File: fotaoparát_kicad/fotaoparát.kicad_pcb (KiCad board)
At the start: 4 copper layers, 115.5 x 68 mm, 64 parts, among them J1 Conn_01x01_Pin, J10 Conn_01x01_Pin, J11 Conn_01x01_Pin, J12 Conn_01x01_Pin, J13 Micro_SD_Card_Det2, J2 Conn_01x01_Pin, J3 Conn_01x01_Pin, J4 Conn_01x01_Pin, J5 Conn_01x01_Pin, J6 Conn_01x01_Pin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

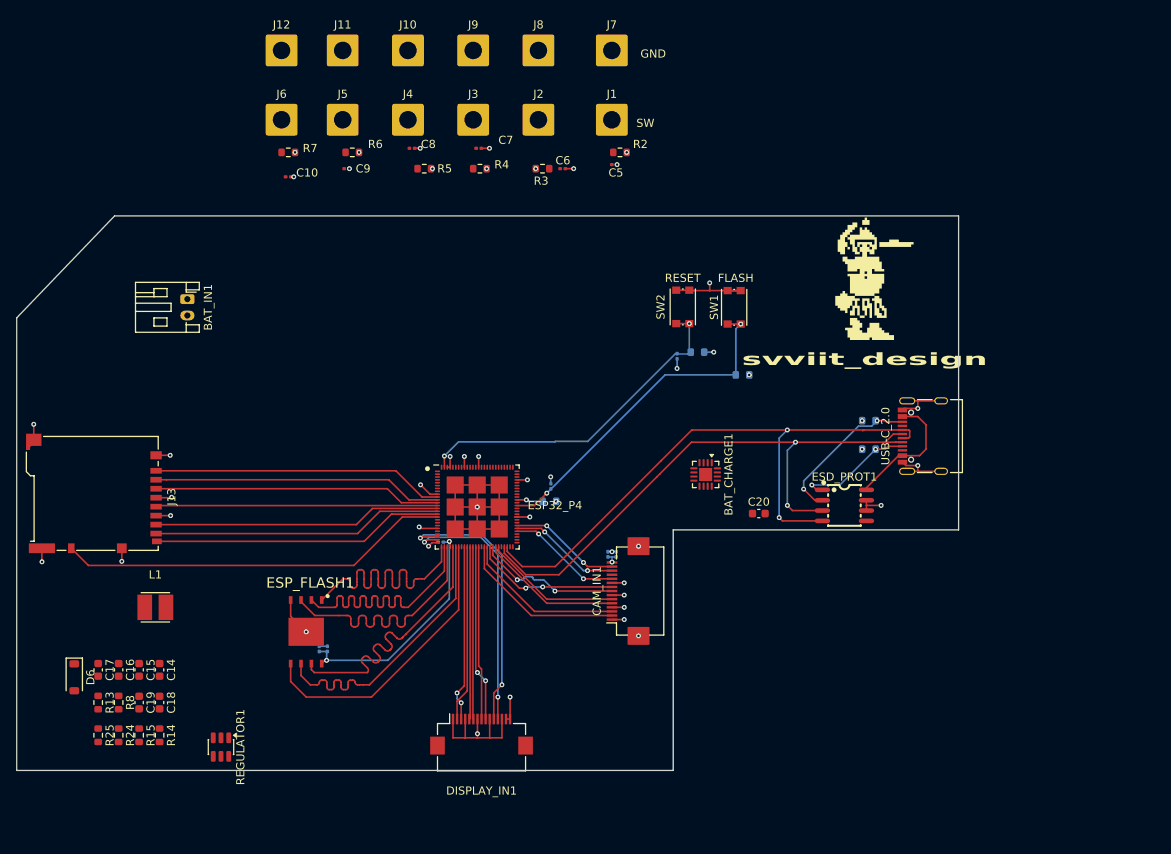
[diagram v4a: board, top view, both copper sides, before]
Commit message: Predelani 80 % routingu pro optimalizaci mista na desce, a predelani napajeni do 7,2V akumulatoru.
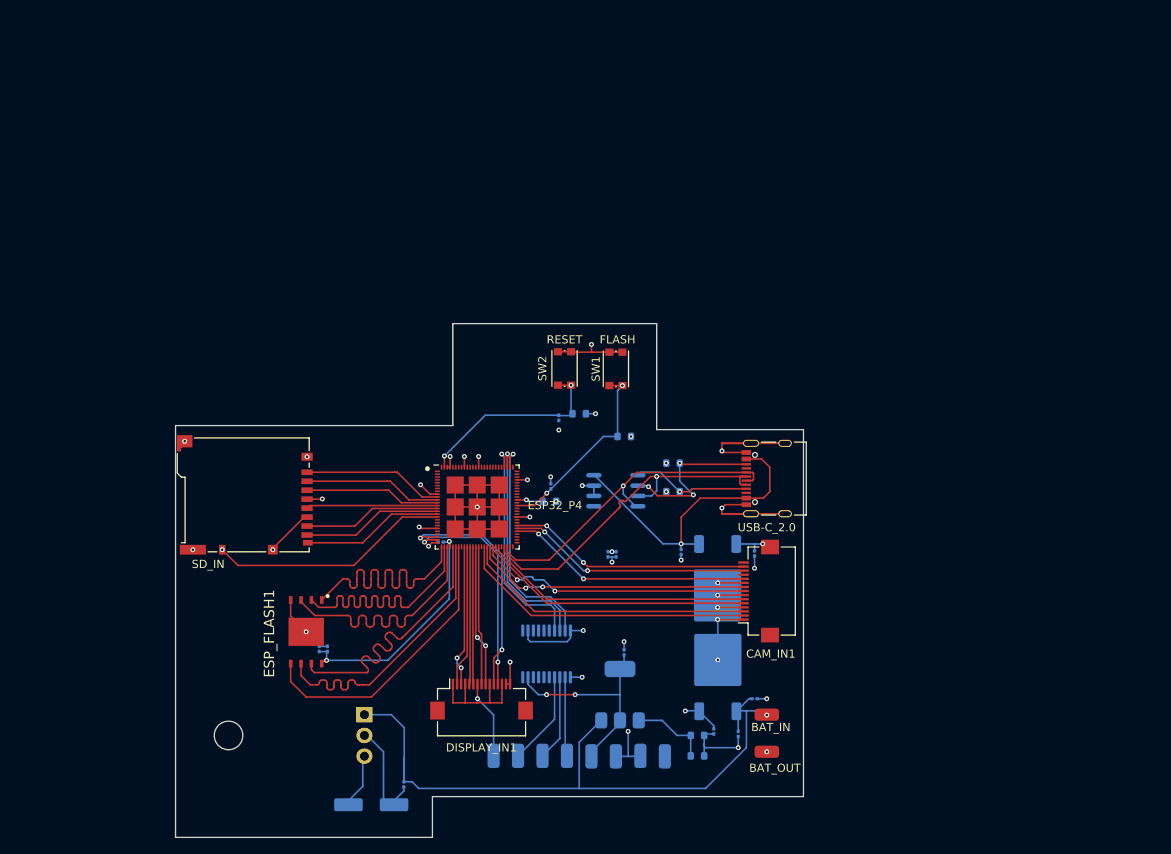
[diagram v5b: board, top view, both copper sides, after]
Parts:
- removed BAT_CHARGE1: BQ24073RGT, Package_DFN_QFN:VQFN-16-1EP_3x3mm_P0.5mm_EP1.6x1.6mm
- removed BAT_IN1: Conn_01x02_Socket, Connector_JST:JST_PH_S2B-PH-K_1x02_P2.00mm_Horizontal
- removed C16, C19: 22uF, Capacitor_SMD:C_0603_1608Metric
- removed C17: 100n, Capacitor_SMD:C_0603_1608Metric
- removed C18, C20: 1u, Capacitor_SMD:C_0603_1608Metric
- removed D6: 3v6 Zener, Diode_SMD:D_SOD-123
- removed J10, J11, J12, J5: Conn_01x01_Pin, Connector_Wire:SolderWire-1.5sqmm_1x01_D1.7mm_OD3.9mm
- removed L1: 4,7uH, stlib:IND-SMD_L3.5-W3.0
- removed R13: 620, Resistor_SMD:R_0603_1608Metric
- removed R14, R24, R25, R4, R5, R6, R7, R8: 10k, Resistor_SMD:R_0603_1608Metric
- removed R15: 1k1, Resistor_SMD:R_0603_1608Metric
- removed REGULATOR1: AP63203WU, Package_TO_SOT_SMD:TSOT-23-6
- added BATT_POW1: BD33FC0FP, Package_TO_SOT_SMD:TO-252-2, B.Cu at (162.5, 118.7)
- added BAT_IN: Conn_01x01_Socket, Connector_Wire:SolderWirePad_1x01_SMD_1.5x3mm, F.Cu at (168.5, 124.2)
- added BAT_OUT: Conn_01x01_Socket, Connector_Wire:SolderWirePad_1x01_SMD_1.5x3mm, F.Cu at (168.5, 128.7)
- added LENS-LOGIC_POW1: AMS1117, Package_TO_SOT_SMD:SOT-223-3_TabPin2, B.Cu at (150.5, 121.7)
- added LENS_POW1: L7806, Package_TO_SOT_THT:TO-220-3_Horizontal_TabDown, B.Cu at (119.1, 124.2)
- added LOGIC_CONVERT1: TXS0108EPW, Package_SO:TSSOP-20_4.4x6.5mm_P0.65mm, B.Cu at (141.5, 116.7)
- added USB_POW1: BD33FC0FP, Package_TO_SOT_SMD:TO-252-2, B.Cu at (162.5, 108.3)
- C10, C5, C6, C8: value 100nF -> 10uF; moved to B.Cu
- C14: value 10uF -> 22uF; footprint Capacitor_SMD:C_0603_1608Metric -> Capacitor_SMD:C_0201_0603Metric; moved to B.Cu
- C15: value 100n -> 22uF; footprint Capacitor_SMD:C_0603_1608Metric -> Capacitor_SMD:C_0201_0603Metric; moved to B.Cu
- C7: value 100nF -> 22uF; moved to B.Cu
- C9: value 100nF -> 100uF; footprint Capacitor_SMD:C_0201_0603Metric -> Capacitor_SMD:CP_Elec_6.3x5.4; moved to B.Cu
- ESD_PROT1, svviit_design: moved to B.Cu
- J1, J2, J3, J4, J6, J7, J8, J9: value Conn_01x01_Pin -> Conn_01x01_Socket; footprint Connector_Wire:SolderWire-1.5sqmm_1x01_D1.7mm_OD3.9mm -> Connector_Wire:SolderWirePad_1x01_SMD_1.5x3mm; moved to B.Cu
- R2: value 10k -> 240; moved to B.Cu
- R3: value 10k -> 820; moved to B.Cu
- moved J9 89.7 mm to (156.0, 129.3), turned to 180 degrees
- moved J6 89.6 mm to (153.0, 129.2), turned to 180 degrees
- moved J8 86.8 mm to (147.0, 129.3), turned to 180 degrees
- moved J7 86.6 mm to (150.0, 129.3), turned to 180 degrees
- moved svviit_design 81.6 mm to (103.2, 96.7), turned to 180 degrees
- moved J4 78.7 mm to (135.0, 129.2), turned to 180 degrees
- moved J1 78.2 mm to (144.0, 129.2), turned to 180 degrees
- moved J3 78.2 mm to (138.0, 129.2), turned to 180 degrees
- moved C9 78.1 mm to (120.0, 135.2)
- moved C8 78.0 mm to (124.0, 132.7), turned to -90 degrees
- moved J2 78.0 mm to (141.0, 129.2), turned to 180 degrees
- moved C15 76.8 mm to (167.0, 104.4)
- moved R2 74.6 mm to (160.0, 129.2), turned to 0 degrees
- moved R3 72.1 mm to (160.0, 126.7)
- moved C5 71.5 mm to (165.0, 126.5), turned to -90 degrees
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- renumbered J13 to SD_IN
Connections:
- C10 pad 1: Net-(ESP32_P4-VDD_IO_5) -> +5V
- C14 pad 1: GND -> +3.3V
- C14 pad 2: +3.3V -> GND
- C15 pad 1: Net-(REGULATOR1-BST) -> +3.3V
- C15 pad 2: Net-(REGULATOR1-SW) -> GND
- C5 pad 1: Net-(ESP32_P4-GPIO39) -> +7V2
- C6 pad 1: Net-(ESP32_P4-GPIO40) -> +7V2
- C7 pad 1: Net-(ESP32_P4-GPIO41) -> +5V5
- C8 pad 1: Net-(ESP32_P4-GPIO42) -> +7V2
- C9 pad 1: Net-(ESP32_P4-GPIO43) -> +6V
- ESP32_P4 pad 83: Net-(ESP32_P4-GPIO42) -> unconnected-(ESP32_P4-GPIO42-Pad83)
- ESP32_P4 pad 84: Net-(ESP32_P4-GPIO43) -> unconnected-(ESP32_P4-GPIO43-Pad84)
- ESP32_P4 pad 85: Net-(ESP32_P4-VDD_IO_5) -> unconnected-(ESP32_P4-VDD_IO_5-Pad85)
- J1 pad 1: Net-(ESP32_P4-GPIO39) -> /DCL
- J2 pad 1: Net-(ESP32_P4-GPIO40) -> /DLC
- J3 pad 1: Net-(ESP32_P4-GPIO41) -> /LCLK
- J4 pad 1: Net-(ESP32_P4-GPIO42) -> GND
- J6 pad 1: Net-(ESP32_P4-VDD_IO_5) -> GND
- J8 pad 1: GND -> +5V5
- J9 pad 1: GND -> +6V
- R2 pad 1: +3.3V -> Net-(LENS-LOGIC_POW1-ADJ)
- R2 pad 2: Net-(ESP32_P4-GPIO39) -> GND
- R3 pad 1: +3.3V -> Net-(LENS-LOGIC_POW1-ADJ)
- R3 pad 2: Net-(ESP32_P4-GPIO40) -> GND
- SW1 pad 1: GND -> Net-(ESP32_P4-GPIO35)
- SW1 pad 2: GND -> Net-(ESP32_P4-GPIO35)
- SW2 pad 1: Net-(ESP32_P4-CHIP_PU) -> GND
- SW2 pad 2: Net-(ESP32_P4-CHIP_PU) -> GND
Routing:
- net +7V2: track 0.00 -> 82.7 mm, vias 0 -> 1
- net GND: track 107.2 -> 173.6 mm
- net Net-(ESD_PROT1-I/O4): track 76.3 -> 40.8 mm, vias 2 -> 1
- net Net-(ESD_PROT1-I/O3): track 72.7 -> 43.3 mm, vias 2 -> 1
- net Net-(ESP32_P4-GPIO39): track 0.00 -> 28.1 mm, vias 0 -> 1
- net Net-(ESP32_P4-GPIO41): track 0.00 -> 27.8 mm, vias 0 -> 1
- net Net-(ESP32_P4-GPIO40): track 0.00 -> 27.7 mm, vias 0 -> 1
- net +5V5: track 0.00 -> 26.7 mm, vias 0 -> 2
- net +5V: track 15.8 -> 38.8 mm, vias 0 -> 1
- net /DET1: track 48.2 -> 29.7 mm, vias 0 -> 1
- net /DAT2: track 35.8 -> 17.3 mm
- net /CMD: track 35.2 -> 16.6 mm
- net /DAT3/CD: track 35.5 -> 16.9 mm
- net /DET2: track 35.8 -> 17.3 mm
- net /CLK: track 34.6 -> 16.1 mm
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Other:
- board size 115.5 x 68 mm -> 77 x 63 mm
- board text removed: "GND"
- board text removed: "SW"

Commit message: vice optimalizace
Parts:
- moved SW1 61.7 mm to (99.5, 117.2)
- moved SW2 52.9 mm to (99.5, 110.8), turned to 90 degrees
- moved R12 52.7 mm to (104.7, 115.2)
- moved R11 46.1 mm to (104.7, 108.7)
- moved C11 46.0 mm to (104.3, 112.7), turned to 0 degrees
- moved C13 44.0 mm to (104.5, 119.2), turned to 0 degrees
- moved C9 10.1 mm to (125.5, 126.7), turned to 90 degrees
- moved C8 8.40 mm to (121.0, 124.9)
- moved DISPLAY_IN1 7.45 mm to (133.5, 129.7)
- moved svviit_design 3.08 mm to (102.5, 93.7)
- moved C1 0.42 mm to (128.7, 103.4), turned to 90 degrees
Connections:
- SW1 pad 1: Net-(ESP32_P4-GPIO35) -> GND
- SW2 pad 2: GND -> Net-(ESP32_P4-CHIP_PU)
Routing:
- net Net-(ESP32_P4-GPIO35): track 24.1 -> 72.6 mm, vias 2 -> 4
- net GND: track 173.6 -> 131.3 mm, vias 29 -> 43
- net +6V: track 6.50 -> 46.1 mm, vias 0 -> 2
- net Net-(ESP32_P4-CHIP_PU): track 24.5 -> 52.9 mm, vias 2 -> 4
- net /DSI_DATAP1: track 17.4 -> 24.9 mm
- net /I2C_SDA: track 27.7 -> 35.2 mm
- net /I2C_SCL: track 29.6 -> 37.0 mm
- net /DSI_DATAP0: track 17.3 -> 24.8 mm
- net /DSI_DATAN0: track 17.0 -> 24.4 mm
- net /DSI_CLKP: track 16.9 -> 24.3 mm
- net /DSI_CLKN: track 16.9 -> 24.3 mm
- net +3V3: track 3.20 -> 10.7 mm
- net /DSI_DATAN1: track 17.4 -> 24.8 mm
- net +3.3V: track 36.1 -> 38.7 mm
- added copper zone on F.Cu, net GND
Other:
- board size 77 x 63 mm -> 77 x 49 mm
